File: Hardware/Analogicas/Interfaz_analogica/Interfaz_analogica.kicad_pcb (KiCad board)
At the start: 2 copper layers, 100 x 100 mm, 34 parts, among them J0 Screw_Terminal_01x07, J1-1 Screw_Terminal_01x01, J1-2 Screw_Terminal_01x01, J2-1 Screw_Terminal_01x01, J2-2 Screw_Terminal_01x01, J3-1 Screw_Terminal_01x01, J3-2 Screw_Terminal_01x01, J4-1 Screw_Terminal_01x01, J4-2 Screw_Terminal_01x01, J5-1 Screw_Terminal_01x01, J5-2 Screw_Terminal_01x01, J6-1 Screw_Terminal_01x01, J6-2 Screw_Terminal_01x01, J7-1 Screw_Terminal_01x01, J7-2 Screw_Terminal_01x01, J8-1 Screw_Terminal_01x01, J8-2 Screw_Terminal_01x01, J9 Screw_Terminal_01x06, Q1 2N2222, Q2 2N2222, Q3 2N2222, Q4 2N2222, U1 LM741, U2 LM741, U3 LM741, U4 LM741

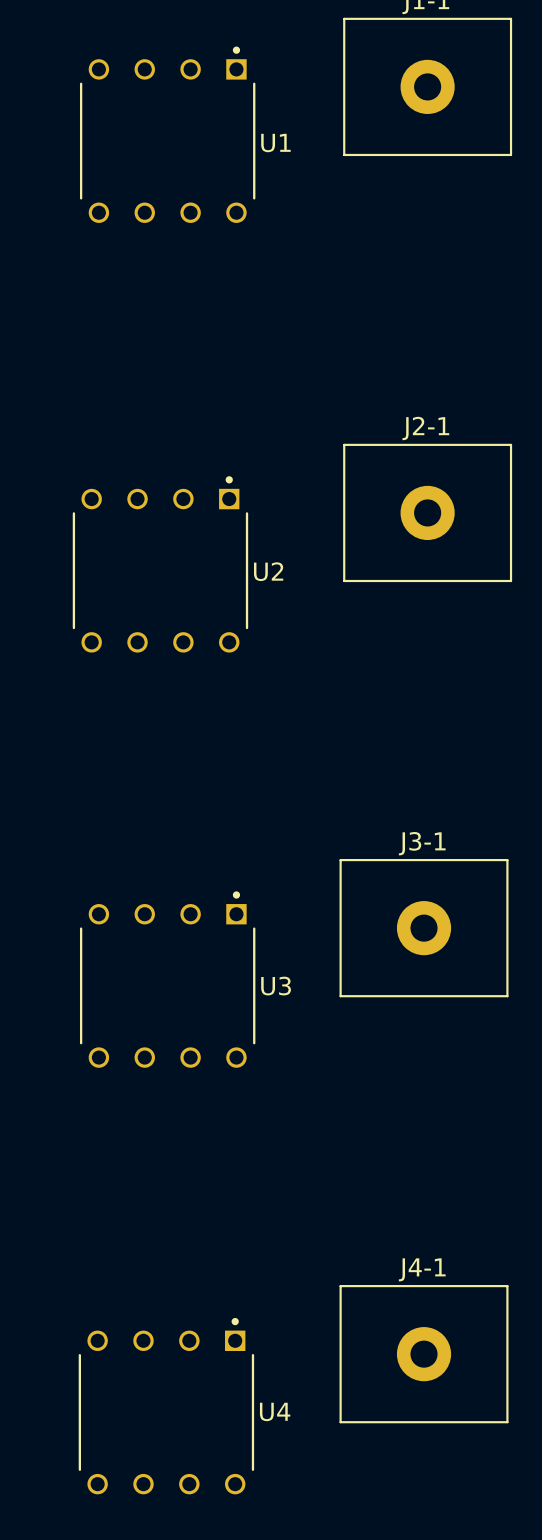
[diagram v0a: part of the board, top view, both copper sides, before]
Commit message: Actualización del codigo del ESP32
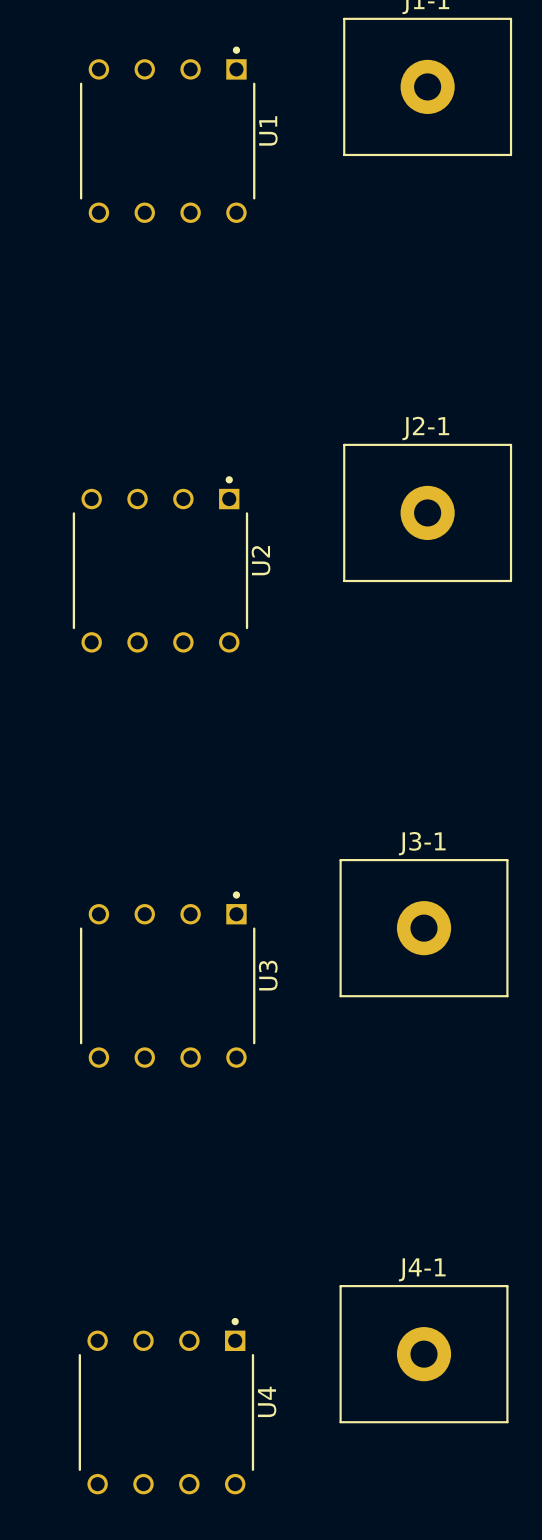
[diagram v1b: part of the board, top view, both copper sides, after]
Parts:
- U1, U2, U3, U4: footprint LM741_TH:LM471_TH -> LM741_TH:LM741_TH
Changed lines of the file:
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@@
 		)
 	)
-	(footprint "LM741_TH:LM471_TH"
+	(footprint "LM741_TH:LM741_TH"
 		(layer "F.Cu")
 		(at 29 60.6 -90)
 		(property "Reference" "U3"
-			(at 0.045 -6 180)
+			(at -0.565 -5.607 270)
 			(layer "F.SilkS")
 			(effects
@@
 		)
 		(property "Value" "LM741"
-			(at 0.135 6 90)
+			(at 10.865 5.607 270)
 			(layer "F.Fab")
 			(effects
@@
 		)
 		(property "Datasheet" "http://www.ti.com/lit/ds/symlink/lm741.pdf"
-			(at 0 0 90)
+			(at 0 0 270)
 			(layer "F.Fab")
 			(hide yes)
@@
 		)
 		(property "Description" "Operational Amplifier, DIP-8/TO-99-8"
-			(at 0 0 90)
+			(at 0 0 270)
 			(layer "F.Fab")
 			(hide yes)
@@
 		)
 		(embedded_fonts no)
-		(model "C:/Users/Bojtronic/Documents/KiCad/9.0/library/LM741/LM741CN_NOPB.step"
+		(model "/home/bojorge/Documents/TEC/TFG/Kicad library/LM741CN_NOPB/LM741CN_NOPB.step"
 			(offset
 				(xyz 0 0 0)
@@
 		)
 	)
-	(footprint "LM741_TH:LM471_TH"
+	(footprint "LM741_TH:LM741_TH"
 		(layer "F.Cu")
 		(at 28.93 84.23 -90)
 		(property "Reference" "U4"
-			(at 0 -6 180)
+			(at -0.565 -5.607 270)
 			(layer "F.SilkS")
 			(effects
@@
 		)
 		(property "Value" "LM741"
-			(at 0.135 6 90)
+			(at 10.865 5.607 270)
 			(layer "F.Fab")
 			(effects
@@
 		)
 		(property "Datasheet" "http://www.ti.com/lit/ds/symlink/lm741.pdf"
-			(at 0 0 90)
+			(at 0 0 270)
 			(layer "F.Fab")
 			(hide yes)
@@
 		)
 		(property "Description" "Operational Amplifier, DIP-8/TO-99-8"
-			(at 0 0 90)
+			(at 0 0 270)
 			(layer "F.Fab")
 			(hide yes)
@@
 		)
 		(embedded_fonts no)
-		(model "C:/Users/Bojtronic/Documents/KiCad/9.0/library/LM741/LM741CN_NOPB.step"
+		(model "/home/bojorge/Documents/TEC/TFG/Kicad library/LM741CN_NOPB/LM741CN_NOPB.step"
 			(offset
 				(xyz 0 0 0)
@@
 		)
 	)
-	(footprint "LM741_TH:LM471_TH"
+	(footprint "LM741_TH:LM741_TH"
 		(layer "F.Cu")
 		(at 28.6 37.6 -90)
 		(property "Reference" "U2"
-			(at 0.09 -6 180)
+			(at -0.565 -5.607 270)
 			(layer "F.SilkS")
 			(effects
@@
 		)
 		(property "Value" "LM741"
-			(at 0.135 6 90)
+			(at 10.865 5.607 270)
 			(layer "F.Fab")
 			(effects
@@
 		)
 		(property "Datasheet" "http://www.ti.com/lit/ds/symlink/lm741.pdf"
-			(at 0 0 90)
+			(at 0 0 270)
 			(layer "F.Fab")
 			(hide yes)
@@
 		)
 		(property "Description" "Operational Amplifier, DIP-8/TO-99-8"
-			(at 0 0 90)
+			(at 0 0 270)
 			(layer "F.Fab")
 			(hide yes)
@@
 		)
 		(embedded_fonts no)
-		(model "C:/Users/Bojtronic/Documents/KiCad/9.0/library/LM741/LM741CN_NOPB.step"
+		(model "/home/bojorge/Documents/TEC/TFG/Kicad library/LM741CN_NOPB/LM741CN_NOPB.step"
 			(offset
 				(xyz 0 0 0)
@@
 		)
 	)
-	(footprint "LM741_TH:LM471_TH"
+	(footprint "LM741_TH:LM741_TH"
 		(layer "F.Cu")
 		(at 29 13.8 -90)
 		(property "Reference" "U1"
-			(at 0.135 -6 180)
+			(at -0.565 -5.607 270)
 			(layer "F.SilkS")
 			(effects
@@
 		)
 		(property "Value" "LM741"
-			(at 0.135 6 90)
+			(at 10.865 5.607 270)
 			(layer "F.Fab")
 			(effects
@@
 		)
 		(property "Datasheet" "http://www.ti.com/lit/ds/symlink/lm741.pdf"
-			(at 0 0 90)
+			(at 0 0 270)
 			(layer "F.Fab")
 			(hide yes)
@@
 		)
 		(property "Description" "Operational Amplifier, DIP-8/TO-99-8"
-			(at 0 0 90)
+			(at 0 0 270)
 			(layer "F.Fab")
 			(hide yes)
@@
 		)
 		(embedded_fonts no)
-		(model "C:/Users/Bojtronic/Documents/KiCad/9.0/library/LM741/LM741CN_NOPB.step"
+		(model "/home/bojorge/Documents/TEC/TFG/Kicad library/LM741CN_NOPB/LM741CN_NOPB.step"
 			(offset
 				(xyz 0 0 0)

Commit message: Creación de PCB's con los archivos gerber y drill
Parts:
- removed J0: Screw_Terminal_01x07, TerminalBlock_Phoenix:TerminalBlock_Phoenix_PT-1,5-7-3.5-H_1x07_P3.50mm_Horizontal
- removed J9: Screw_Terminal_01x06, TerminalBlock_Phoenix:TerminalBlock_Phoenix_PT-1,5-6-3.5-H_1x06_P3.50mm_Horizontal
- added J0_1: Screw_Terminal_01x03, TerminalBlock_Phoenix:TerminalBlock_Phoenix_PT-1,5-3-3.5-H_1x03_P3.50mm_Horizontal, F.Cu at (-12.5, 34.0)
- added J0_2: Screw_Terminal_01x03, TerminalBlock_Phoenix:TerminalBlock_Phoenix_PT-1,5-3-3.5-H_1x03_P3.50mm_Horizontal, F.Cu at (-12.5, 46.5)
- added J0_3: Screw_Terminal_01x03, TerminalBlock_Phoenix:TerminalBlock_Phoenix_PT-1,5-3-3.5-H_1x03_P3.50mm_Horizontal, F.Cu at (-12.5, 59.0)
- added J9_1: Screw_Terminal_01x03, TerminalBlock_Phoenix:TerminalBlock_Phoenix_PT-1,5-3-3.5-H_1x03_P3.50mm_Horizontal, F.Cu at (86.3, 47.5)
- added J9_2: Screw_Terminal_01x03, TerminalBlock_Phoenix:TerminalBlock_Phoenix_PT-1,5-3-3.5-H_1x03_P3.50mm_Horizontal, F.Cu at (86.5, 60.0)
- moved H1 24.2 mm to (-18.0, 6.21)
- moved H4 23.6 mm to (-18.0, 93.8)
- moved J5-2 13.4 mm to (65.8, 23.3)
- moved J6-2 13.4 mm to (65.8, 46.5)
- moved J7-1 13.4 mm to (49.8, 68.7)
- moved J7-2 13.4 mm to (66.0, 69.1)
- moved J8-2 13.4 mm to (65.8, 92.1)
- moved Q1 13.4 mm to (61.8, 13.6)
- moved Q4 13.4 mm to (61.0, 84.0)
- moved J3-1 13.4 mm to (29.8, 58.1)
- moved J4-1 13.4 mm to (29.8, 81.7)
- moved C1 13.4 mm to (0.01, 32.7)
- moved C2 13.4 mm to (0.01, 43.7)
- moved C3 13.4 mm to (0.01, 54.7)
- moved C4 13.4 mm to (0.01, 65.7)
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- renumbered H1 to H4
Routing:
- net GNDREF: track 0.00 -> 226.5 mm, vias 0 -> 1
- net Net-(J0_1-Pin_1): track 0.00 -> 129.1 mm
- net Net-(J9_1-Pin_3): track 0.00 -> 115.2 mm
- net Net-(J0_1-Pin_2): track 0.00 -> 111.8 mm
- net Net-(J5-2-Pin_1): track 0.00 -> 49.9 mm, vias 0 -> 1
- net Net-(J8-2-Pin_1): track 0.00 -> 45.7 mm
- net Net-(J0_3-Pin_1): track 0.00 -> 43.9 mm
- net Net-(J0_2-Pin_1): track 0.00 -> 42.3 mm
- net Net-(J7-2-Pin_1): track 0.00 -> 36.3 mm
- net Net-(J6-2-Pin_1): track 0.00 -> 34.6 mm
- net Net-(J0_2-Pin_3): track 0.00 -> 30.5 mm
- net Net-(J0_2-Pin_2): track 0.00 -> 29.0 mm
- net Net-(J4-1-Pin_1): track 0.00 -> 21.6 mm
- net Net-(J3-1-Pin_1): track 0.00 -> 21.2 mm
- net Net-(J2-1-Pin_1): track 0.00 -> 20.7 mm
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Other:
- board size 100 x 100 mm -> 125 x 100 mm

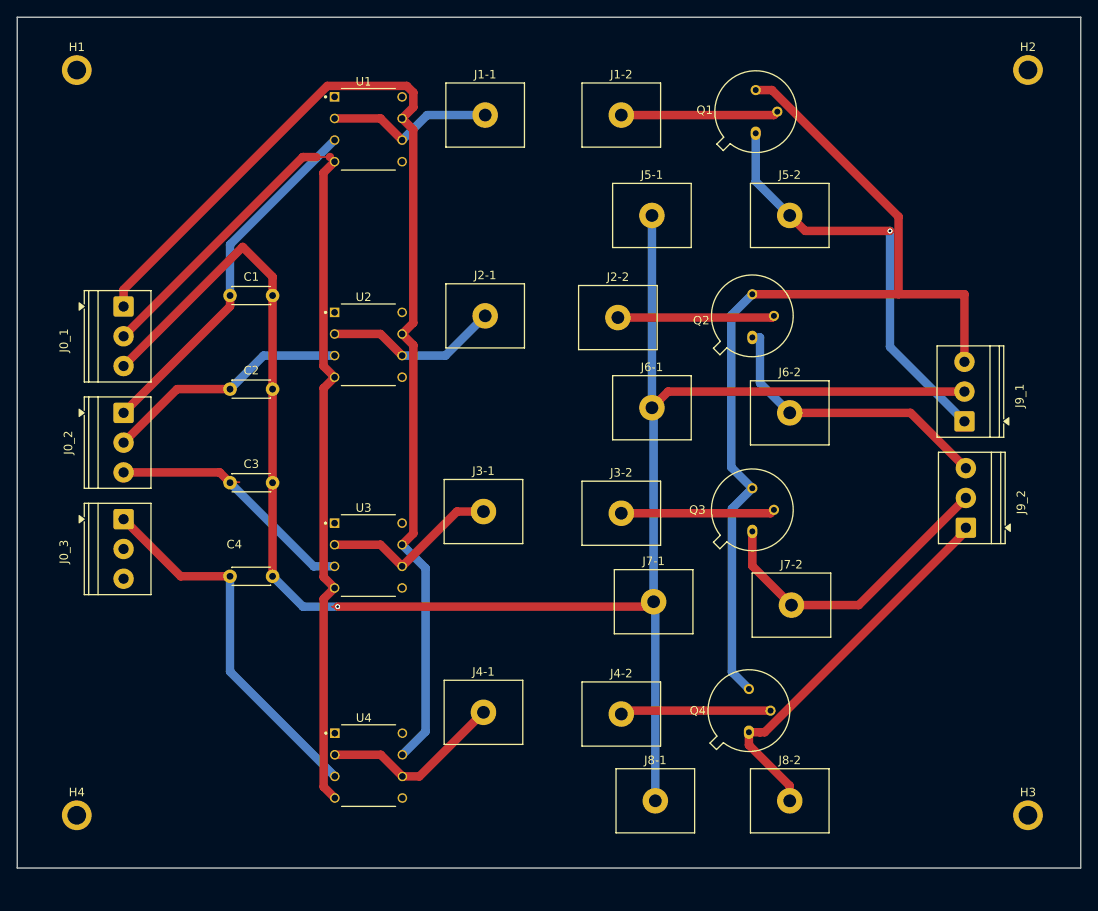
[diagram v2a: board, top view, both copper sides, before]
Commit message: Agregando agujeros para montaje a las PCB
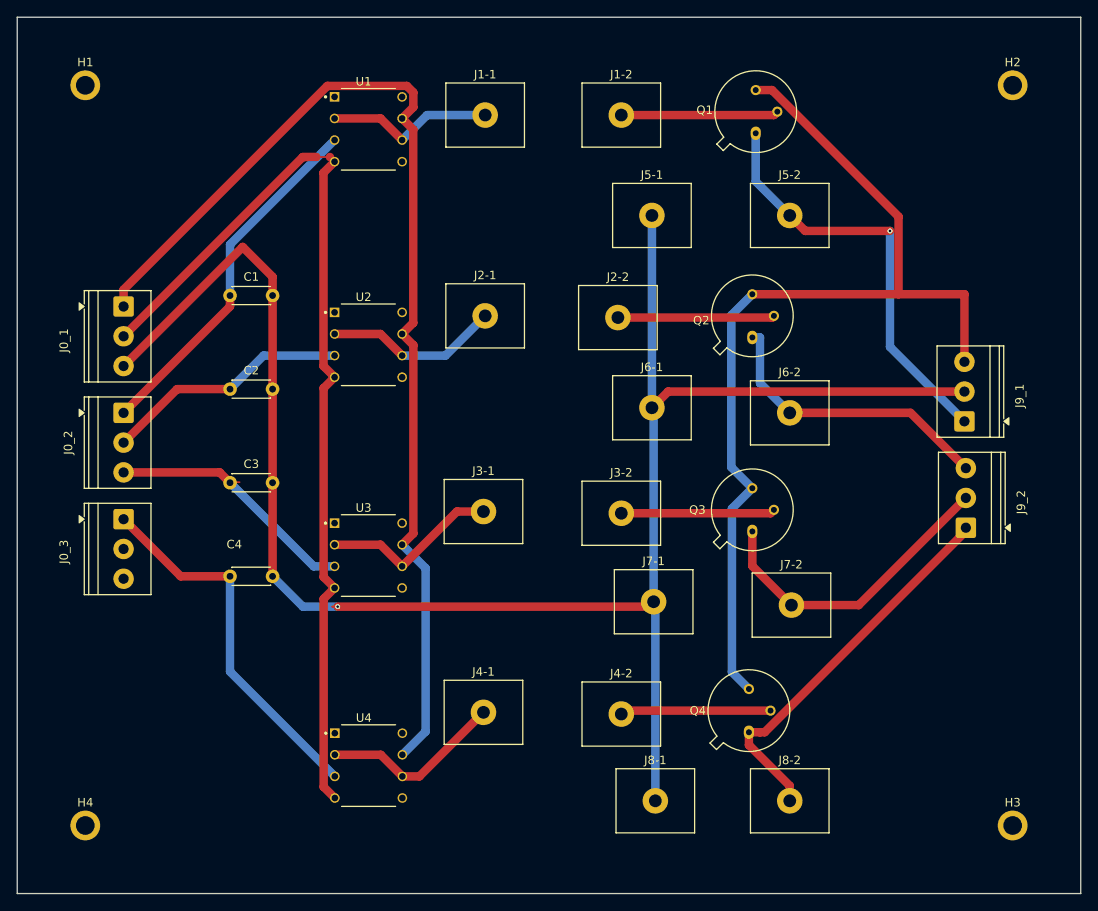
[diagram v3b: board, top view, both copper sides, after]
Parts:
- moved H2 2.55 mm to (92.0, 8.00)
- moved H3 2.16 mm to (92.0, 95.0)
- moved H1 2.05 mm to (-17.0, 8.00)
- moved H4 1.56 mm to (-17.0, 95.0)
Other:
- board size 125 x 100 mm -> 125 x 103 mm
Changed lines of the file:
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@@
 	(footprint "MountingHole:MountingHole_2.2mm_M2_ISO7380_Pad"
 		(layer "F.Cu")
-		(at -18 93.8)
+		(at -17 95)
 		(descr "Mounting Hole 2.2mm, M2, generated by kicad-footprint-generator mountinghole.py")
 		(tags "mountinghole M2 ISO7380")
@@
 	(footprint "MountingHole:MountingHole_2.2mm_M2_ISO7380_Pad"
 		(layer "F.Cu")
-		(at 93.8 93.8)
+		(at 92 95)
 		(descr "Mounting Hole 2.2mm, M2, generated by kicad-footprint-generator mountinghole.py")
 		(tags "mountinghole M2 ISO7380")
@@
 	(footprint "MountingHole:MountingHole_2.2mm_M2_ISO7380_Pad"
 		(layer "F.Cu")
-		(at -18 6.212)
+		(at -17 8)
 		(descr "Mounting Hole 2.2mm, M2, generated by kicad-footprint-generator mountinghole.py")
 		(tags "mountinghole M2 ISO7380")
@@
 	(footprint "MountingHole:MountingHole_2.2mm_M2_ISO7380_Pad"
 		(layer "F.Cu")
-		(at 93.8 6.2)
+		(at 92 8)
 		(descr "Mounting Hole 2.2mm, M2, generated by kicad-footprint-generator mountinghole.py")
 		(tags "mountinghole M2 ISO7380")
@@
 	)
 	(gr_line
-		(start 100 100)
-		(end -25 100)
+		(start 100 103)
+		(end -25 103)
 		(stroke
 			(width 0.05)
@@
 	)
 	(gr_line
-		(start -25 100)
+		(start -25 103)
 		(end -25 0)
 		(stroke
@@
 	(gr_line
 		(start 100 0)
-		(end 100 100)
+		(end 100 103)
 		(stroke
 			(width 0.05)

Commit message: Ruteo de la interfaz analógica
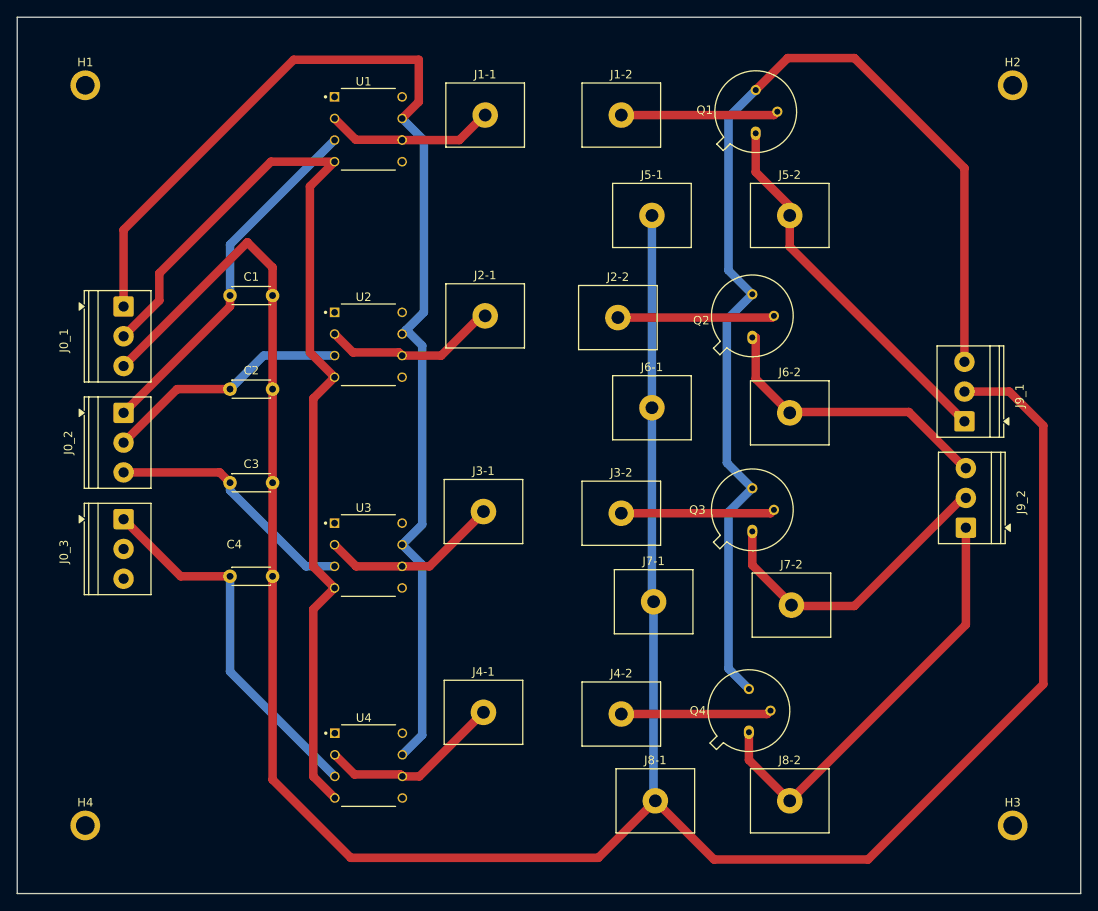
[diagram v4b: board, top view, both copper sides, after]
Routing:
- net GNDREF: track 226.5 -> 303.8 mm, vias 1 -> 0
- net Net-(J9_1-Pin_3): track 115.2 -> 131.7 mm
- net Net-(J0_1-Pin_1): track 129.1 -> 140.9 mm
- net Net-(J5-2-Pin_1): track 49.9 -> 44.0 mm, vias 1 -> 0
- net Net-(J8-2-Pin_1): track 45.7 -> 50.7 mm
- net Net-(J0_1-Pin_2): track 111.8 -> 116.5 mm
- net Net-(J0_2-Pin_3): track 30.5 -> 29.9 mm

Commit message: Ajustes a las interfaces digital y analogica
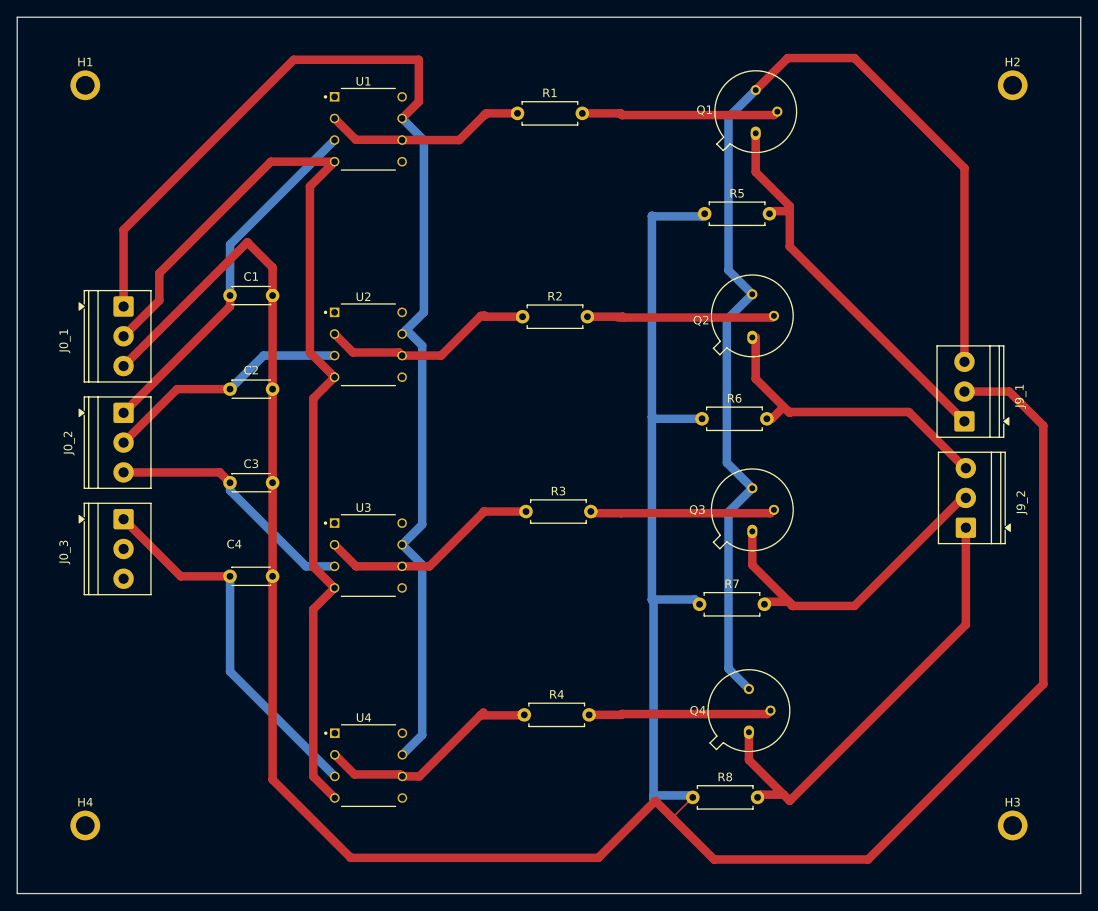
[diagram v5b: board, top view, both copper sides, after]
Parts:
- removed J1-1, J1-2, J2-1, J2-2, J3-1, J3-2, J4-1, J4-2, J5-1, J5-2, J6-1, J6-2, J7-1, J7-2, J8-1, J8-2: Screw_Terminal_01x01, TerminalBlock_MetzConnect:TerminalBlock_MetzConnect_360271_1x01_Horizontal_ScrewM3.0_Boxed
- added R1: R_US, Resistor_THT:R_Axial_DIN0207_L6.3mm_D2.5mm_P7.62mm_Horizontal, F.Cu at (33.8, 11.3)
- added R2: R_US, Resistor_THT:R_Axial_DIN0207_L6.3mm_D2.5mm_P7.62mm_Horizontal, F.Cu at (34.4, 35.2)
- added R3: R_US, Resistor_THT:R_Axial_DIN0207_L6.3mm_D2.5mm_P7.62mm_Horizontal, F.Cu at (34.8, 58.1)
- added R4: R_US, Resistor_THT:R_Axial_DIN0207_L6.3mm_D2.5mm_P7.62mm_Horizontal, F.Cu at (34.6, 82.0)
- added R5: R_US, Resistor_THT:R_Axial_DIN0207_L6.3mm_D2.5mm_P7.62mm_Horizontal, F.Cu at (55.8, 23.1)
- added R6: R_US, Resistor_THT:R_Axial_DIN0207_L6.3mm_D2.5mm_P7.62mm_Horizontal, F.Cu at (55.5, 47.2)
- added R7: R_US, Resistor_THT:R_Axial_DIN0207_L6.3mm_D2.5mm_P7.62mm_Horizontal, F.Cu at (55.2, 69.0)
- added R8: R_US, Resistor_THT:R_Axial_DIN0207_L6.3mm_D2.5mm_P7.62mm_Horizontal, F.Cu at (54.4, 91.7)
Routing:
- net GNDREF: track 303.8 -> 330.1 mm
- net Net-(U4--): track 21.6 -> 26.8 mm
- net Net-(U3--): track 21.3 -> 26.3 mm
- net Net-(Q1-B): track 18.5 -> 23.3 mm
- net Net-(U2--): track 20.7 -> 25.3 mm
- net Net-(Q2-B): track 18.4 -> 22.7 mm
- net Net-(U1--): track 20.0 -> 24.0 mm
- net Net-(Q4-B): track 17.7 -> 21.7 mm
- net Net-(Q3-B): track 18.1 -> 21.8 mm
- net Net-(J9_2-Pin_1): track 50.7 -> 53.9 mm
- net Net-(J9_2-Pin_3): track 34.4 -> 37.5 mm
- net Net-(J9_2-Pin_2): track 36.4 -> 39.4 mm
- net Net-(J9_1-Pin_1): track 44.0 -> 46.5 mm
